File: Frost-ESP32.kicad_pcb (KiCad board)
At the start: 4 copper layers, 50 x 50 mm, 29 parts, among them J1 Micro_SD_Card, J2 CAN, J3 USB_C_Receptacle, J4 Conn_01x10, SW1 SW_Push, U2 AP2112K-3.3, U3 TJA1051T-3, U4 ESP32-C3-WROOM-02

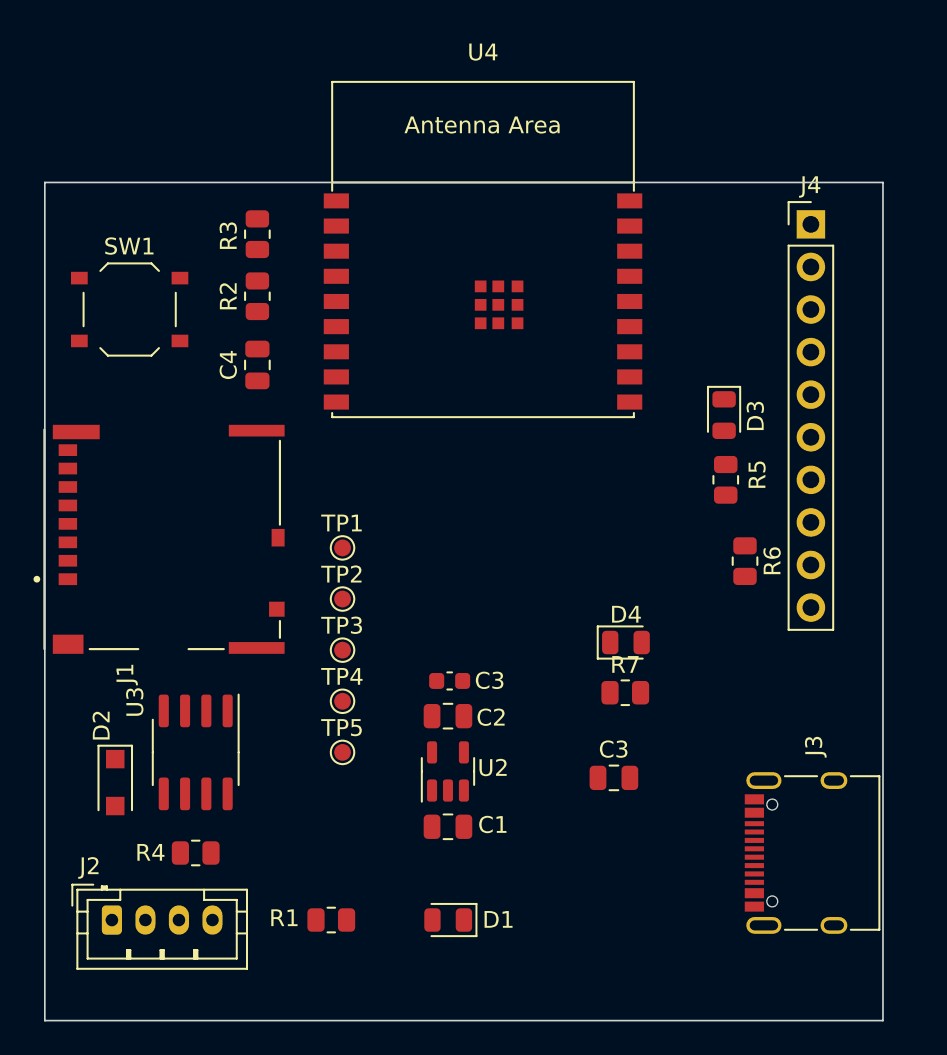
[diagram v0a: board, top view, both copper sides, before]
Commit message: moved some symbols to fair library
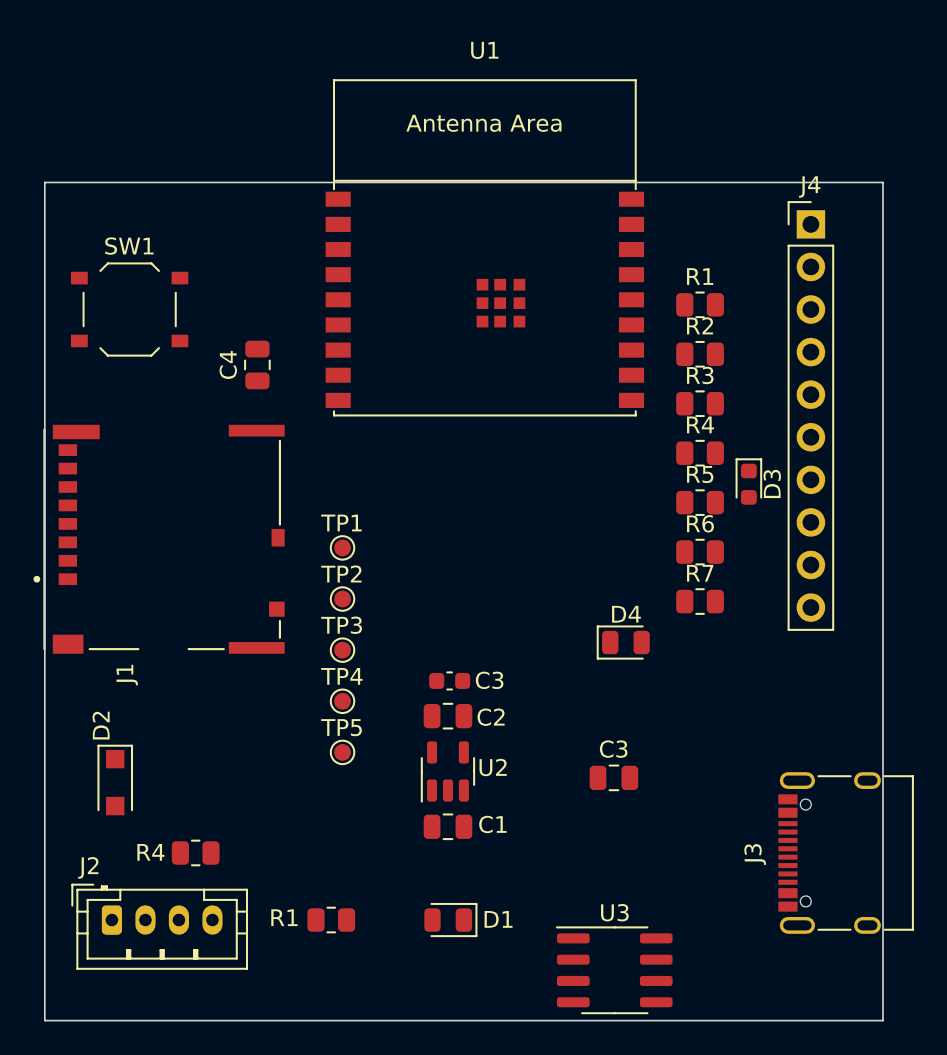
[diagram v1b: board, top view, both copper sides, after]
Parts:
- removed U4: ESP32-C3-WROOM-02, espressif:ESP32-C3-WROOM-02
- added R1: 1k, Resistor_SMD:R_0805_2012Metric, F.Cu at (133.1, 68.3)
- added R4: R_0805_220, Resistor_SMD:R_0805_2012Metric, F.Cu at (133.1, 77.2)
- added U1: ESP32-C3-WROOM-02, Fair:ESP32-C3-WROOM-02, F.Cu at (120.2, 67.9)
- D3: footprint LED_SMD:LED_0805_2012Metric -> LED_SMD:LED_0603_1608Metric
- J3: value USB_C_Receptacle -> USB_C_Receptacle_USB2.0
- R2: value 10k -> R_0805_10k
- moved R3 28.3 mm to (133.1, 74.2), turned to 0 degrees
- moved U3 28.2 mm to (128.0, 108.0), turned to 0 degrees
- moved R2 26.6 mm to (133.1, 71.2), turned to 0 degrees
- moved R7 7.03 mm to (133.1, 86.0)
- moved D3 4.38 mm to (136.0, 79.0)
- moved R6 2.74 mm to (133.1, 83.0), turned to 0 degrees
- moved R5 2.05 mm to (133.1, 80.1), turned to 0 degrees
- moved J3 2.00 mm to (142.0, 101.0)
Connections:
- C4 pad 1: Net-(U4-EN/CHIP_PU) -> Net-(U1-EN/CHIP_PU)
- R2 pad 1: Net-(U4-EN/CHIP_PU) -> +3V3
- R2 pad 2: +3V3 -> Net-(U1-EN/CHIP_PU)
- R5 pad 1: /LED_BLUE -> Net-(D4-A)
- R5 pad 2: Net-(D3-A) -> /LED_RED
- R6 pad 1: Net-(U4-GPIO8) -> /GPIO8
- R7 pad 1: /LED_RED -> Net-(D3-A)
- R7 pad 2: Net-(D4-A) -> /LED_BLUE

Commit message: After ordering v0.1
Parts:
- removed the C3 at (118.2, 90.7)
- removed the C3 at (128.0, 96.5)
- removed C4: 1u, Capacitor_SMD:C_0805_2012Metric
- removed J4: Conn_01x10, Connector_PinHeader_2.54mm:PinHeader_1x10_P2.54mm_Vertical
- removed the R1 at (133.1, 68.3)
- removed the R1 at (111.1, 105.0)
- removed the R4 at (133.1, 77.2)
- removed the R4 at (103.0, 101.0)
- removed SW1: SW_Push, Button_Switch_SMD:SW_Push_1P1T_XKB_TS-1187A
- added C3: 1uF/25V, Capacitor_SMD:C_0402_1005Metric, F.Cu at (108.1, 108.1)
- added D5: 100V/3A, Diode_SMD:D_SOD-123F, F.Cu at (142.1, 100.0)
- added H1: MountingHole, MountingHole:MountingHole_3.2mm_M3, F.Cu at (104.0, 107.0)
- added H2: MountingHole, MountingHole:MountingHole_3.2mm_M3, F.Cu at (138.0, 107.0)
- added R1: 1k, Resistor_SMD:R_0402_1005Metric, F.Cu at (141.7, 103.3)
- added R4: 220, Resistor_SMD:R_0402_1005Metric, F.Cu at (99.8, 101.2)
- added S1: TL3340AF160QG, Fair:SW_TL3340AF160QG, F.Cu at (106.7, 99.8)
- added TP6: TestPoint, TestPoint:TestPoint_Pad_D1.0mm, F.Cu at (110.7, 108.2)
- added TP7: TestPoint, TestPoint:TestPoint_Pad_D1.0mm, F.Cu at (109.5, 109.9)
- C1, C2: value 10uF -> 10uF/6.3V; footprint Capacitor_SMD:C_0805_2012Metric -> Capacitor_SMD:C_0402_1005Metric
- D1: value RED -> Red; footprint LED_SMD:LED_0805_2012Metric -> LED_SMD:LED_0603_1608Metric
- D3: value BLUE -> Blue
- D4: value RED -> Emerald; footprint LED_SMD:LED_0805_2012Metric -> LED_SMD:LED_0603_1608Metric
- J1: footprint espressif:MOLEX_503398-1892 -> Fair:MOLEX_503398-1892; moved to B.Cu
- J2: footprint Connector_JST:JST_PH_B4B-PH-K_1x04_P2.00mm_Vertical -> Connector_PinHeader_1.27mm:PinHeader_1x10_P1.27mm_Vertical
- J3: value USB_C_Receptacle_USB2.0 -> USB__B_Micro_Horizontal; footprint Connector_USB:USB_C_Receptacle_XKB_U262-16XN-4BVC11 -> Connector_USB:USB_Micro-B_Molex_47346-0001; moved to B.Cu
- R2: value R_0805_10k -> 10k; footprint Resistor_SMD:R_0805_2012Metric -> Resistor_SMD:R_0402_1005Metric
- R3, R5, R6, R7: footprint Resistor_SMD:R_0805_2012Metric -> Resistor_SMD:R_0402_1005Metric
- U2, U3: moved to B.Cu
- moved R2 42.9 mm to (108.1, 106.1), turned to 90 degrees
- moved R6 38.7 mm to (99.8, 102.8), turned to 180 degrees
- moved R7 37.8 mm to (99.8, 103.9), turned to 180 degrees
- moved U1 35.8 mm to (122.5, 103.7)
- moved J1 31.5 mm to (124.0, 103.8), turned to -90 degrees
- moved D3 31.0 mm to (143.0, 109.2)
- moved R5 30.9 mm to (141.5, 109.8), turned to 90 degrees
- moved R3 30.7 mm to (142.8, 103.3), turned to 90 degrees
- moved TP2 30.5 mm to (138.0, 101.3)
- moved U3 29.1 mm to (99.9, 100.6), turned to 180 degrees
- moved TP3 26.7 mm to (135.4, 101.3)
- moved C2 23.6 mm to (99.5, 107.5), turned to 180 degrees
- moved D4 22.7 mm to (143.0, 106.0), turned to -90 degrees
- moved U2 21.9 mm to (100.0, 108.5)
- moved C1 20.8 mm to (99.5, 108.9), turned to 180 degrees
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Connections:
- net Net-(D2-A) renamed /Vconn
- R2 pad 1: +3V3 -> Net-(U1-EN/CHIP_PU)
- R2 pad 2: Net-(U1-EN/CHIP_PU) -> +3V3
- R3 pad 2: /LED_RED -> /LED_Green
- R5 pad 1: Net-(D4-A) -> Net-(D3-A)
- R5 pad 2: /LED_RED -> /LED_Blue
- R6 pad 1: /GPIO8 -> +3V3
- R6 pad 2: +3V3 -> /GPIO8
- R7 pad 1: Net-(D3-A) -> +3V3
- R7 pad 2: /LED_BLUE -> Net-(D1-A)
- U1 pad 15: /LED_BLUE -> /LED_Blue
- U1 pad 16: /LED_RED -> /LED_Green
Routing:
- net +5V: track 0.00 -> 78.4 mm, vias 0 -> 3
- net /TX: track 0.00 -> 49.0 mm, vias 0 -> 3
- net /RX: track 0.00 -> 44.9 mm, vias 0 -> 3
- net /GPIO10: track 0.00 -> 44.7 mm, vias 0 -> 1
- net GND: track 0.00 -> 44.3 mm, vias 0 -> 13
- net /CAN_RX: track 0.00 -> 31.8 mm, vias 0 -> 2
- net /CAN_TX: track 0.00 -> 29.6 mm, vias 0 -> 2
- net /GPIO8: track 0.00 -> 20.8 mm, vias 0 -> 2
- net /LED_Blue: track 0.00 -> 19.3 mm
- net /USB_D-: track 0.00 -> 15.3 mm, vias 0 -> 1
- net /LED_Green: track 0.00 -> 14.6 mm
- net /CANH: track 0.00 -> 14.3 mm, vias 0 -> 1
- net /CANL: track 0.00 -> 14.1 mm, vias 0 -> 1
- net /USB_D+: track 0.00 -> 13.7 mm, vias 0 -> 1
- net /Vconn: track 0.00 -> 12.8 mm, vias 0 -> 1
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- added copper zone on In2.Cu, net +3V3
- added copper zone on In1.Cu, net GND
- added copper zone on In4.Cu, net GND
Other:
- board size 50 x 50 mm -> 50 x 14.5 mm
- copper layers 4 -> 6
- board text added: "3V3"
- board text added: "5V In"
- board text added: "5V Out"
- board text added: "CANH"
- board text added: "CANL"
- board text added: "C_H"
- board text added: "C_L"
- board text added: "D+"
- board text added: "D-"
- board text added: "GND"
- board text added: "IO08"
- board text added: "IO10"
- board text added: "RX"
- board text added: "TX"
